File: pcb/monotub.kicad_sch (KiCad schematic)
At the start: 13 parts, among them J1 Barrel_Jack, SW1 RST, U1 ESP32-WROOM-32D, U2 V7805-1000, U3 AP7361C-33E

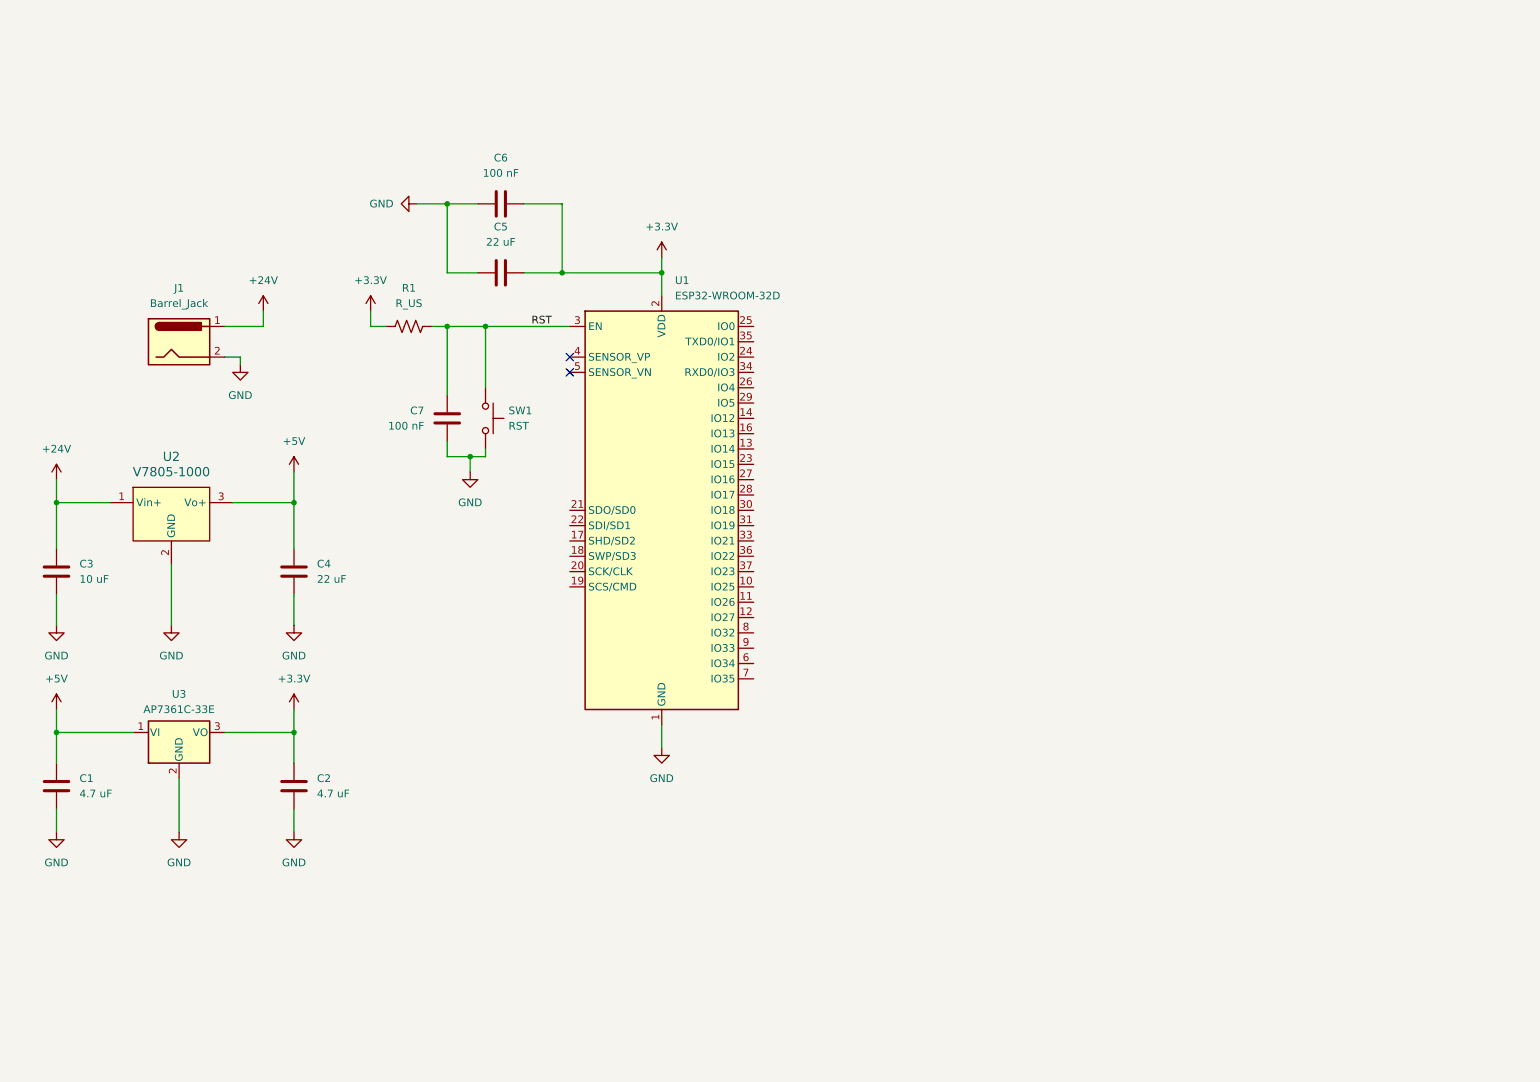
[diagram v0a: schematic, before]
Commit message: Update schematic with fan, humidifier, and other components.
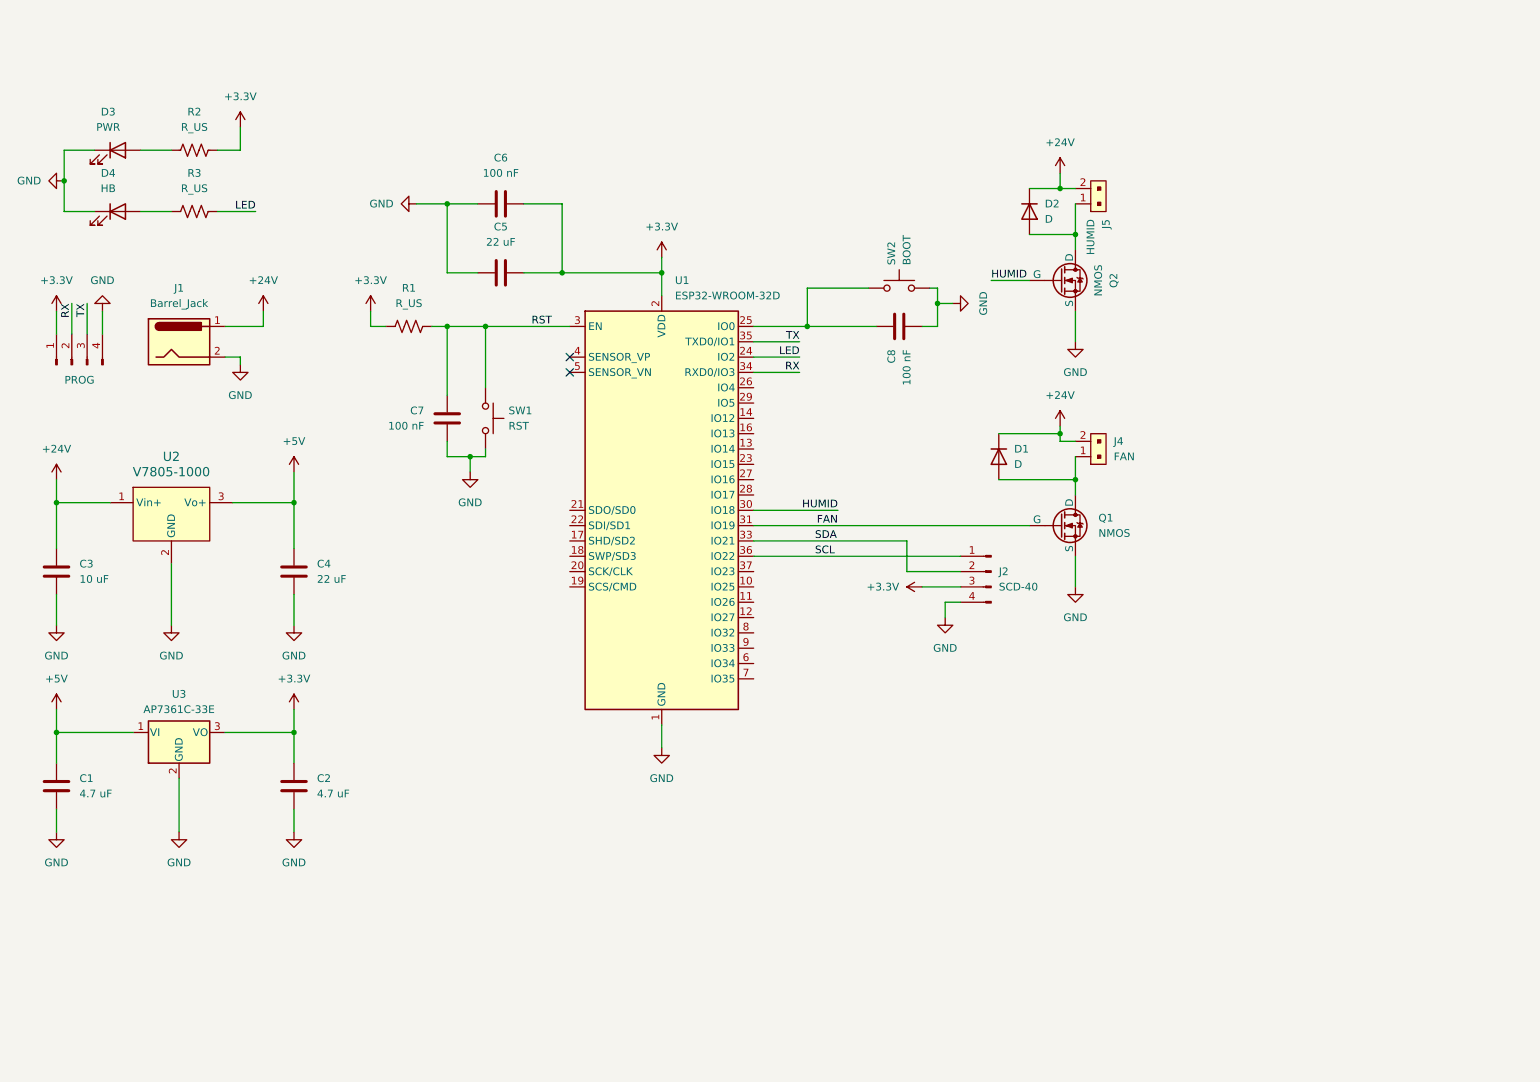
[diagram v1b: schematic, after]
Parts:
- added C8: 100 nF, symbol Device:C
- added D1, D2: D, symbol Device:D
- added D3: PWR, symbol Device:LED
- added D4: HB, symbol Device:LED
- added J2: SCD-40, symbol Connector:Conn_01x04_Pin
- added J3: PROG, symbol Connector:Conn_01x04_Pin
- added J4: FAN, digikey-footprints:PinHeader_1x2_P2mm, symbol dk_Rectangular-Connectors-Headers-Male-Pins:B2B-PH-SM4-TB_LF__SN_
- added J5: HUMID, digikey-footprints:PinHeader_1x2_P2mm, symbol dk_Rectangular-Connectors-Headers-Male-Pins:B2B-PH-SM4-TB_LF__SN_
- added Q1, Q2: NMOS, symbol Simulation_SPICE:NMOS
- added R2, R3: R_US, symbol Device:R_US
- added SW2: BOOT, symbol Switch:SW_Push
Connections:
- net +24V: now also D1.1 (K), D2.1 (K), J4.2, J5.2
- net +3.3V: now also J2.3 (Pin_3), J3.1 (Pin_1), R2.2
- net GND: now also C8.2, D3.1 (K), D4.1 (K), J2.4 (Pin_4), J3.4 (Pin_4), Q1.3 (S), Q2.3 (S), SW2.2
- net LED: now reaches U1.24 (IO2)
- net LED: now also R3.2
- net at U1.25 (IO0): now also C8.1, SW2.1
- net HUMID: now reaches U1.30 (IO18)
- net HUMID: now also Q2.2 (G)
- net FAN: now reaches U1.31 (IO19)
- net FAN: now also Q1.2 (G)
- net SDA: now reaches U1.33 (IO21)
- net SDA: now also J2.2 (Pin_2)
- net RX: now reaches U1.34 (RXD0/IO3)
- net RX: now also J3.2 (Pin_2)
- net TX: now reaches U1.35 (TXD0/IO1)
- net TX: now also J3.3 (Pin_3)
- net SCL: now reaches U1.36 (IO22)
- net SCL: now also J2.1 (Pin_1)
- new net: D2.2 (A), J5.1, Q2.1 (D)
- new net: D3.2 (A), R2.1
- new net: D4.2 (A), R3.1
- new net: D1.2 (A), J4.1, Q1.1 (D)

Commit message: Update schematic with regulator for uC and LED seperate
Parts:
- removed D1: D, symbol Device:D
- added C10, C9: 22 uF, symbol Device:C
- added D5: D_Schottky, symbol Device:D_Schottky
- added J6: LEDS, symbol Connector:Conn_01x03_Socket
- added U4: VR20S05, symbol regulators:VR20S05
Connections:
- net +24V: now also C10.1, D5.1 (K), U4.1 (Vin)
- net GND: now also C10.2, C9.2, J6.3 (Pin_3), U4.2 (GND)
- net at U1.37 (IO23): now also J6.2 (Pin_2)
- net at J4.1, Q1.1 (D): now also D5.2 (A)
- new net +5V_LED: C9.1, J6.1 (Pin_1), U4.3 (Vout)
- no-connect marks 2 -> 23
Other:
- moved on the sheet: D3, D4, R2, R3

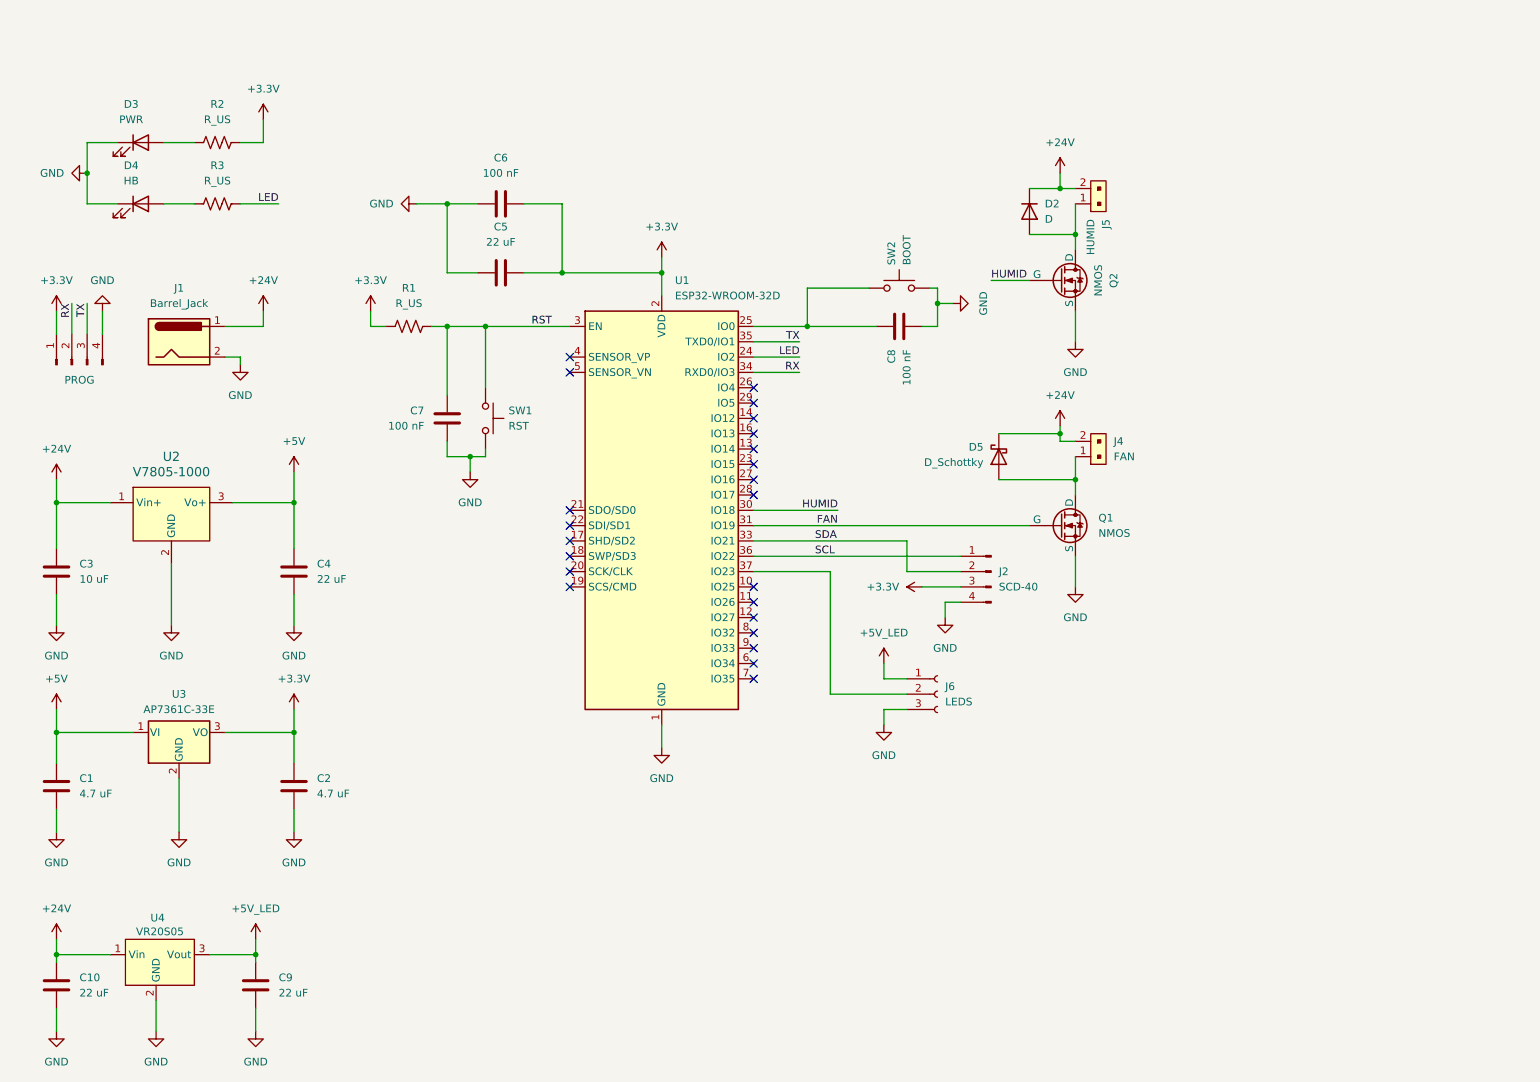
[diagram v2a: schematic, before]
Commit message: Add connectors for water level, pump, and RGB leds
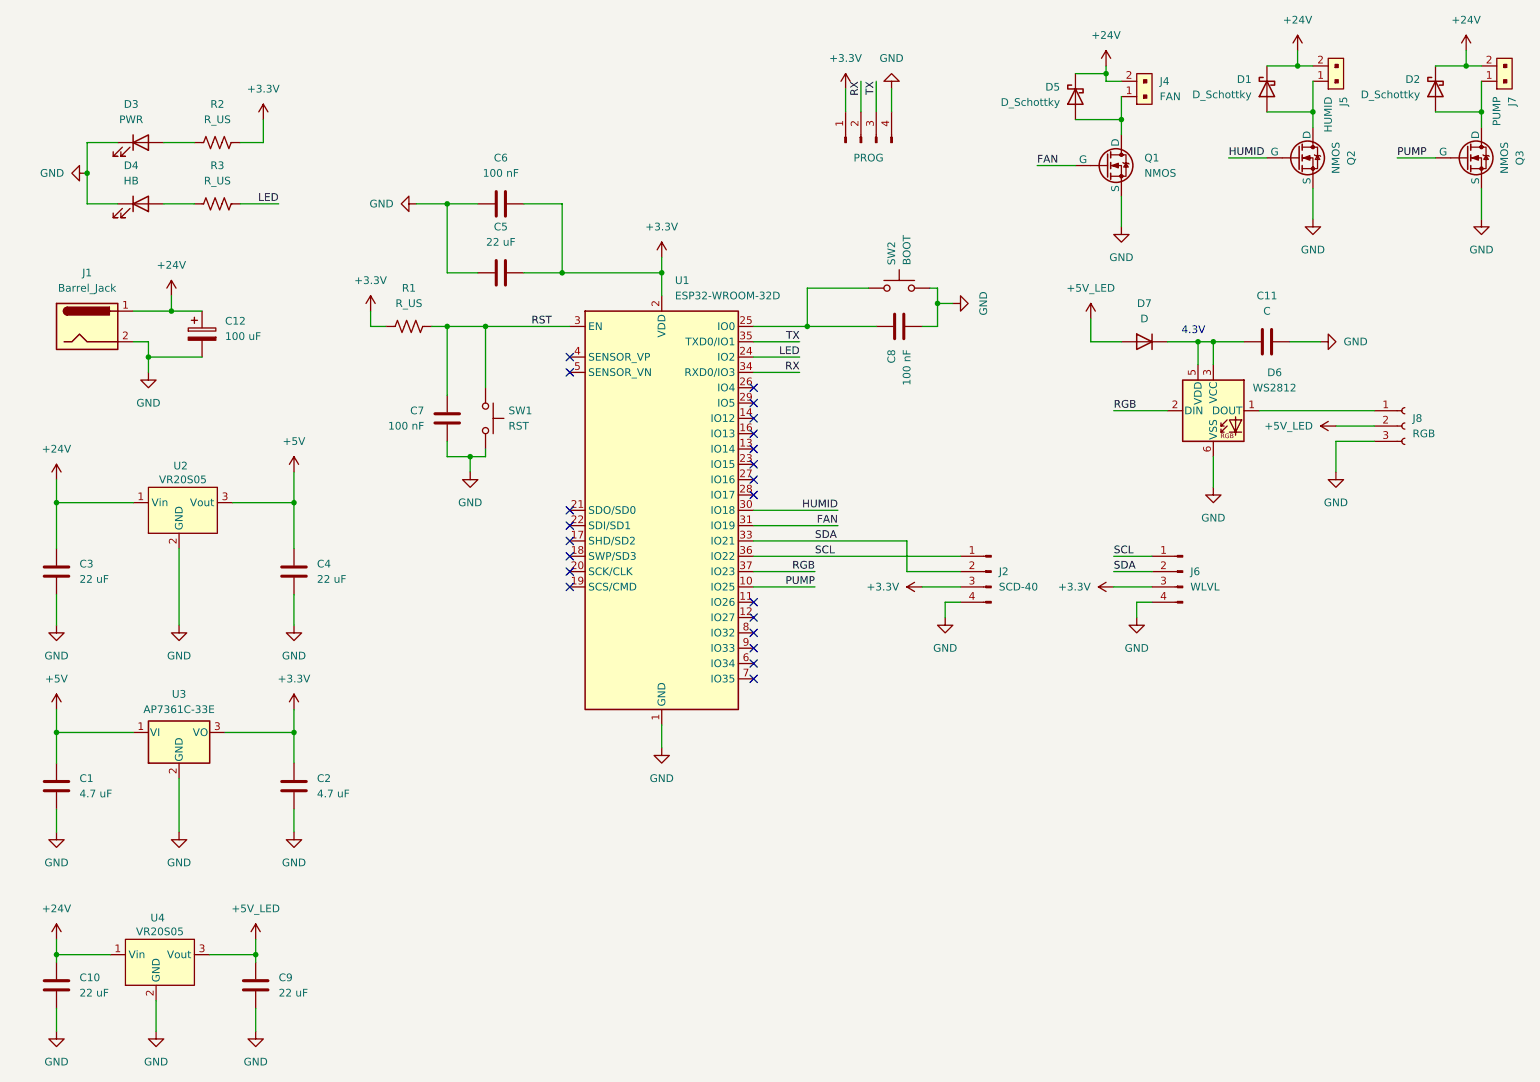
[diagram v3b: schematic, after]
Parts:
- removed D2: D, symbol Device:D
- removed J6: LEDS, symbol Connector:Conn_01x03_Socket
- removed U2: V7805-1000, digikey-footprints:3-SIP_Module_V7805-1000, symbol dk_DC-DC-Converters:V7805-1000
- added C11: C, symbol Device:C
- added C12: 100 uF, symbol Device:C_Polarized
- added D1, D2: D_Schottky, symbol Device:D_Schottky
- added D6: WS2812, LED_SMD:LED_WS2812_PLCC6_5.0x5.0mm_P1.6mm, symbol LED:WS2812
- added D7: D, symbol Device:D
- added J6: WLVL, symbol Connector:Conn_01x04_Pin
- added J7: PUMP, digikey-footprints:PinHeader_1x2_P2mm, symbol dk_Rectangular-Connectors-Headers-Male-Pins:B2B-PH-SM4-TB_LF__SN_
- added J8: RGB, symbol Connector:Conn_01x03_Socket
- added Q3: NMOS, symbol Simulation_SPICE:NMOS
- added U2: VR20S05, symbol regulators:VR20S05
- C3: value 10 uF -> 22 uF
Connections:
- net +24V: now also C12.1, D1.1 (K), D2.1 (K), J7.2, U2.1 (Vin)
- net +3.3V: now also J6.3 (Pin_3)
- net +5V: now also U2.3 (Vout)
- net +5V_LED: now also D7.2 (A), J8.2 (Pin_2)
- net GND: now also C11.2, C12.2, D6.6 (VSS), J6.4 (Pin_4), J8.3 (Pin_3), Q3.3 (S), U2.2 (GND)
- net SCL: now also J6.1 (Pin_1)
- net SDA: now also J6.2 (Pin_2)
- net PUMP: now reaches U1.10 (IO25)
- net PUMP: now also Q3.2 (G)
- net RGB: now reaches U1.37 (IO23)
- net RGB: now also D6.2 (DIN)
- net at J5.1, Q2.1 (D): now also D1.2 (A)
- new net: D6.1 (DOUT), J8.1 (Pin_1)
- new net: D2.2 (A), J7.1, Q3.1 (D)
- new net: C11.1, D6.3 (VCC), D6.5 (VDD), D7.1 (K)
- no-connect marks 23 -> 22
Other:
- note added: "4.3V"
- moved on the sheet: D5, J1, J4, J5, Q1, Q2
